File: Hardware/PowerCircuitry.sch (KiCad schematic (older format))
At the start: 37 parts, among them J4 Conn_01x02_Male, Q5 MTP3055VL, Q6 MTP3055VL, Q7 2N2219, SW3 SW_SPST, U4 MAX40200AUK

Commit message: Added lots of things - needs some redoing
Fun, but ffs could have been easier
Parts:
- removed Q7: 2N2219, Package_TO_SOT_THT:TO-92_Inline, symbol Transistor_BJT:2N2219
- removed SW3: SW_SPST, Button_Switch_THT:SW_DIP_SPSTx01_Slide_9.78x4.72mm_W7.62mm_P2.54mm, symbol Switch:SW_SPST
- added J6: Conn_01x02_Male, Connector_PinHeader_2.54mm:PinHeader_1x02_P2.54mm_Vertical, symbol Connector:Conn_01x02_Male
- added JP1: Jumper_2_Open, Connector_PinHeader_2.54mm:PinHeader_1x02_P2.54mm_Vertical, symbol Jumper:Jumper_2_Open
- added Q7: Q_NMOS_GDS, Package_TO_SOT_SMD:SOT-23, symbol Device:Q_NMOS_GDS
- Q5, Q6: footprint Package_TO_SOT_THT:TO-220-3_Vertical -> Package_TO_SOT_SMD:SOT-23
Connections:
- net 12VBusSwitch: now also Q7.1 (G)
- net GND: now also Q7.3 (S); no longer J4.1 (Pin_1)
- net at C1.1.1, L1.1: now also C2.1.1, L2.1, R21.2, U4.5 (OUT)
- net at Battery1.1 (Pin_1): now also J6.2 (Pin_2)
- net at U4.1 (VDD), U4.3 (EN): now also J6.1 (Pin_1)
- new net: J4.1 (Pin_1), JP1.2 (B)
- new net: JP1.1 (A), Q7.2 (D)
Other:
- moved on the sheet: C1.1
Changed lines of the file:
@@
 EESchema Schematic File Version 4
+LIBS:VLAD-cache
 EELAYER 30 0
 EELAYER END
@@
 	0    -1   -1   0
 $EndComp
-Wire Wire Line
-	2950 1250 3150 1250
 $Comp
 L power:GND #PWR036
 U 1 1 607A1CEB
-P 2950 1550
-F 0 "#PWR036" H 2950 1300 50  0001 C CNN
-F 1 "GND" H 2955 1377 50  0000 C CNN
-F 2 "" H 2950 1550 50  0001 C CNN
-F 3 "" H 2950 1550 50  0001 C CNN
-	1    2950 1550
+P 2750 3450
+F 0 "#PWR036" H 2750 3200 50  0001 C CNN
+F 1 "GND" H 2755 3277 50  0000 C CNN
+F 2 "" H 2750 3450 50  0001 C CNN
+F 3 "" H 2750 3450 50  0001 C CNN
+	1    2750 3450
 	1    0    0    -1
 $EndComp
@@
 L Device:CP1 C1.1
 U 1 1 607A0DAB
-P 2950 1400
-F 0 "C1.1" H 3065 1446 50  0000 L CNN
-F 1 "68uF" H 3065 1355 50  0000 L CNN
-F 2 "Capacitor_THT:CP_Radial_D6.3mm_P2.50mm" H 2950 1400 50  0001 C CNN
-F 3 "~" H 2950 1400 50  0001 C CNN
-	1    2950 1400
-	1    0    0    -1
+P 2600 3450
+F 0 "C1.1" H 2715 3496 50  0000 L CNN
+F 1 "68uF" H 2715 3405 50  0000 L CNN
+F 2 "Capacitor_THT:CP_Radial_D6.3mm_P2.50mm" H 2600 3450 50  0001 C CNN
+F 3 "~" H 2600 3450 50  0001 C CNN
+	1    2600 3450
+	0    -1   -1   0
 $EndComp
 $Comp
@@
 L power:GND #PWR055
 U 1 1 609E5451
-P 9050 3100
-F 0 "#PWR055" H 9050 2850 50  0001 C CNN
-F 1 "GND" H 9055 2927 50  0000 C CNN
-F 2 "" H 9050 3100 50  0001 C CNN
-F 3 "" H 9050 3100 50  0001 C CNN
-	1    9050 3100
+P 9050 3900
+F 0 "#PWR055" H 9050 3650 50  0001 C CNN
+F 1 "GND" H 9055 3727 50  0000 C CNN
+F 2 "" H 9050 3900 50  0001 C CNN
+F 3 "" H 9050 3900 50  0001 C CNN
+	1    9050 3900
 	1    0    0    -1
 $EndComp
 Connection ~ 1100 3750
-$Comp
-L Switch:SW_SPST SW3
-U 1 1 608DCB23
-P 1300 3750
-F 0 "SW3" H 1300 3985 50  0000 C CNN
-F 1 "SW_SPST" H 1300 3894 50  0000 C CNN
-F 2 "Button_Switch_THT:SW_DIP_SPSTx01_Slide_9.78x4.72mm_W7.62mm_P2.54mm" H 1300 3750 50  0001 C CNN
-F 3 "~" H 1300 3750 50  0001 C CNN
-	1    1300 3750
-	1    0    0    -1
-$EndComp
 Wire Wire Line
 	2050 3750 2050 4250
@@
 Wire Wire Line
 	4500 3550 4600 3550
-$Comp
-L Transistor_BJT:2N2219 Q7
-U 1 1 60A91052
-P 2550 3250
-F 0 "Q7" H 2741 3204 50  0000 L CNN
-F 1 "2N2219" H 2741 3295 50  0000 L CNN
-F 2 "Package_TO_SOT_THT:TO-92_Inline" H 2750 3175 50  0001 L CIN
-F 3 "http://www.onsemi.com/pub_link/Collateral/2N2219-D.PDF" H 2550 3250 50  0001 L CNN
-	1    2550 3250
-	-1   0    0    1
-$EndComp
 Wire Wire Line
 	2450 3450 2450 3750
-Wire Wire Line
-	2450 3050 2450 1250
-Wire Wire Line
-	2450 1250 2950 1250
-Connection ~ 2950 1250
-Text GLabel 2750 3250 2    50   Input ~ 0
-12VBusSwitch
 $Comp
 L Device:R R21
@@
 F 0 "Q5" H 1400 1770 50  0000 C CNN
 F 1 "MTP3055VL" H 1400 1679 50  0000 C CNN
-F 2 "Package_TO_SOT_THT:TO-220-3_Vertical" H 1400 1500 50  0001 L BNN
+F 2 "Package_TO_SOT_SMD:SOT-23" H 1400 1500 50  0001 L BNN
 F 3 "" H 1400 1500 50  0001 L BNN
 F 4 "MTP3055VL" H 1400 1500 50  0001 L BNN "MPN"
@@
 F 0 "Q6" H 1400 2520 50  0000 C CNN
 F 1 "MTP3055VL" H 1400 2429 50  0000 C CNN
-F 2 "Package_TO_SOT_THT:TO-220-3_Vertical" H 1400 2250 50  0001 L BNN
+F 2 "Package_TO_SOT_SMD:SOT-23" H 1400 2250 50  0001 L BNN
 F 3 "" H 1400 2250 50  0001 L BNN
 F 4 "MTP3055VL" H 1400 2250 50  0001 L BNN "MPN"
@@
 Text Label 4350 4250 1    50   ~ 0
 Source2
+$Comp
+L Connector:Conn_01x02_Male J6
+U 1 1 60AE4D44
+P 1500 3550
+F 0 "J6" V 1562 3594 50  0000 L CNN
+F 1 "Conn_01x02_Male" V 1653 3594 50  0000 L CNN
+F 2 "Connector_PinHeader_2.54mm:PinHeader_1x02_P2.54mm_Vertical" H 1500 3550 50  0001 C CNN
+F 3 "~" H 1500 3550 50  0001 C CNN
+	1    1500 3550
+	0    1    1    0
+$EndComp
+Wire Wire Line
+	1100 3750 1400 3750
+Connection ~ 2450 3450
+Wire Wire Line
+	2450 1250 3150 1250
+Wire Wire Line
+	2450 1250 2450 3450
+$Comp
+L Device:Q_NMOS_GDS Q7
+U 1 1 60B1F303
+P 8950 3700
+F 0 "Q7" H 9156 3746 50  0000 L CNN
+F 1 "Q_NMOS_GDS" H 9156 3655 50  0000 L CNN
+F 2 "Package_TO_SOT_SMD:SOT-23" H 9150 3800 50  0001 C CNN
+F 3 "~" H 8950 3700 50  0001 C CNN
+	1    8950 3700
+	1    0    0    -1
+$EndComp
+Text GLabel 8750 3700 0    50   Input ~ 0
+12VBusSwitch
+$Comp
+L Jumper:Jumper_2_Open JP1
+U 1 1 60B321AD
+P 9050 3300
+F 0 "JP1" V 9096 3212 50  0000 R CNN
+F 1 "Jumper_2_Open" V 9005 3212 50  0000 R CNN
+F 2 "Connector_PinHeader_2.54mm:PinHeader_1x02_P2.54mm_Vertical" H 9050 3300 50  0001 C CNN
+F 3 "~" H 9050 3300 50  0001 C CNN
+	1    9050 3300
+	0    -1   -1   0
+$EndComp
 $EndSCHEMATC

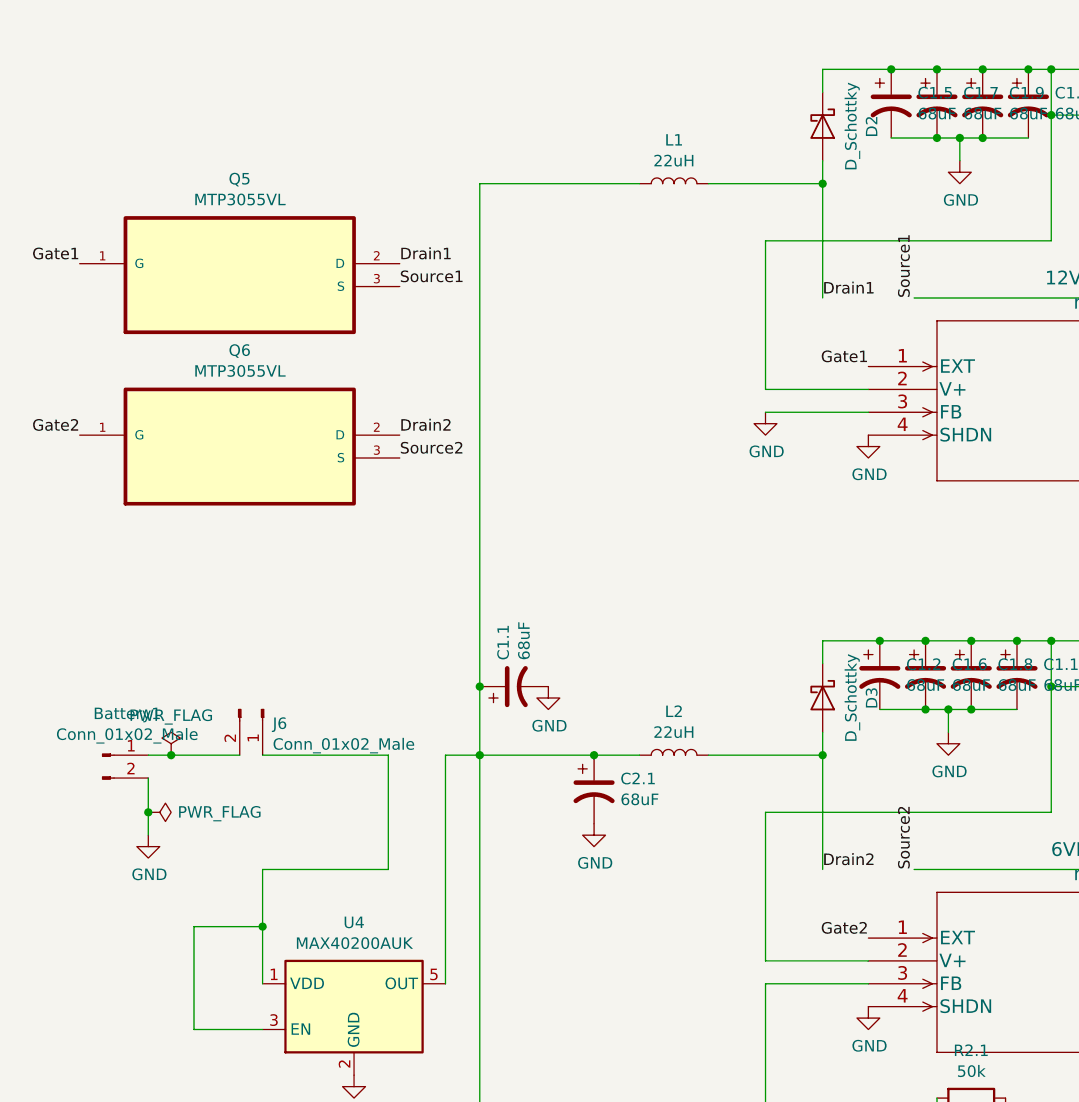
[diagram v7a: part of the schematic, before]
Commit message: Added bunch of vias
Now need to connect some more tracks up and we're good to proceed to adding ground planes etc. Also decreased the size of the board to fit within 90mm x 80mm, have further opportunities to potentially squeeze it.
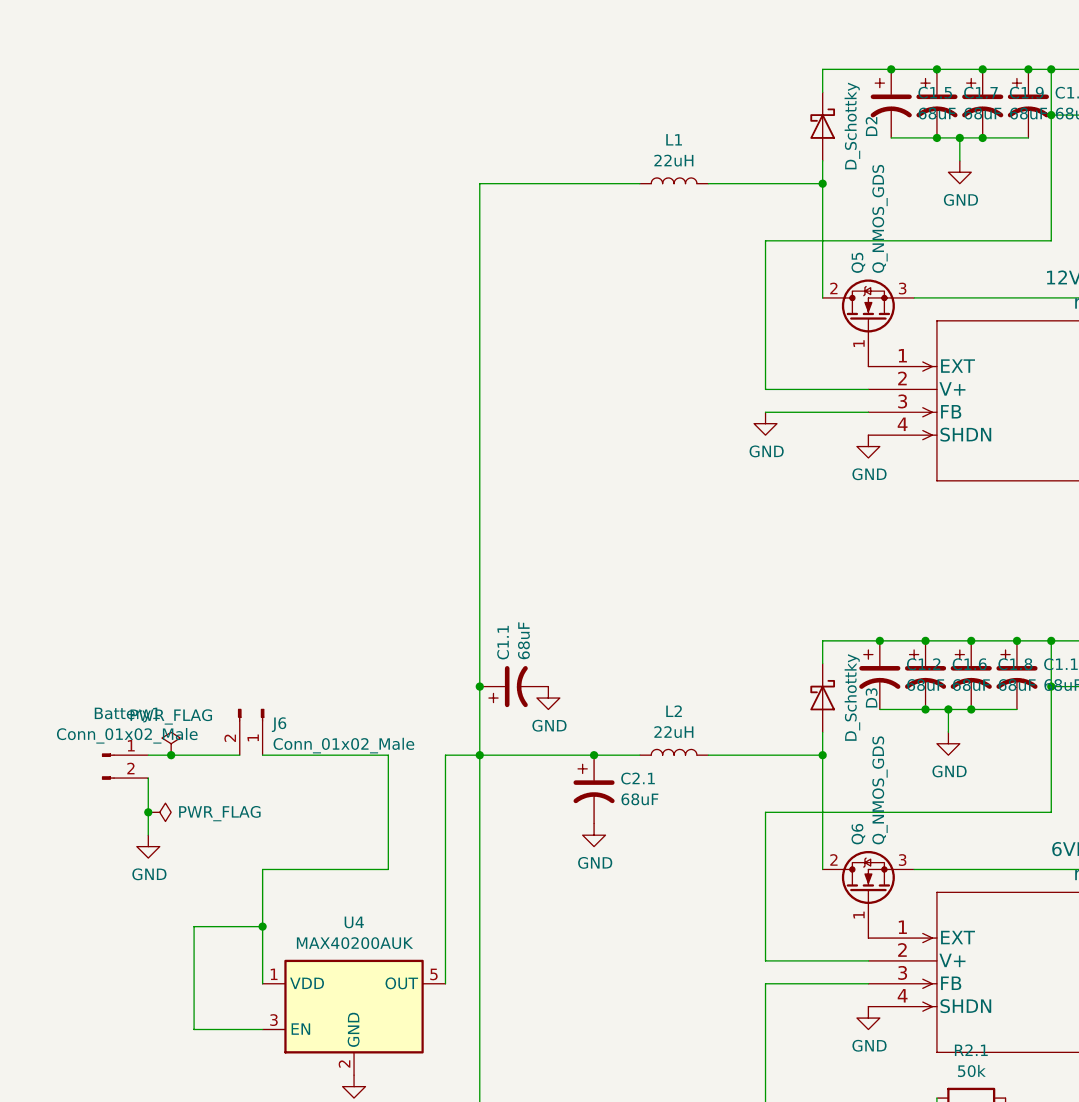
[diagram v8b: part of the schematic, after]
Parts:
- removed Q5, Q6: MTP3055VL, Package_TO_SOT_SMD:SOT-23, symbol VLAD-rescue:MTP3055VL-MTP3055VL
- added Q5, Q6: Q_NMOS_GDS, Package_TO_SOT_SMD:SOT-23, symbol Device:Q_NMOS_GDS
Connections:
- net Drain1: no longer names the net of D2.2 (A), L1.2
- net Drain1: now also Q5.2 (D)
- net Drain2: no longer names the net of D3.2 (A), L2.2
- net Drain2: now also Q6.2 (D)
- net Gate1: no longer names the net of 12VBoostConverter1.1 (EXT)
- net Gate1: now also Q5.1 (G)
- net Gate2: no longer names the net of 6VBoostConverter1.1 (EXT)
- net Gate2: now also Q6.1 (G)
- net Source1: no longer names the net of 12VBoostConverter1.8 (CS), RSense1.1
- net Source1: now also Q5.3 (S)
- net Source2: no longer names the net of 6VBoostConverter1.8 (CS), RSense2.1
- net Source2: now also Q6.3 (S)
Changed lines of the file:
@@
 	2950 6500 3200 6500
-$Comp
-L VLAD-rescue:MTP3055VL-MTP3055VL Q5
-U 1 1 60AA2630
-P 1400 1500
-F 0 "Q5" H 1400 1770 50  0000 C CNN
-F 1 "MTP3055VL" H 1400 1679 50  0000 C CNN
-F 2 "Package_TO_SOT_SMD:SOT-23" H 1400 1500 50  0001 L BNN
-F 3 "" H 1400 1500 50  0001 L BNN
-F 4 "MTP3055VL" H 1400 1500 50  0001 L BNN "MPN"
-F 5 "18C7756" H 1400 1500 50  0001 L BNN "OC_NEWARK"
-F 6 "1845563" H 1400 1500 50  0001 L BNN "OC_FARNELL"
-F 7 "Fairchild" H 1400 1500 50  0001 L BNN "SUPPLIER"
-F 8 "TO-220" H 1400 1500 50  0001 L BNN "PACKAGE"
-	1    1400 1500
-	1    0    0    -1
-$EndComp
-Text Label 700  1600 2    50   ~ 0
-Gate1
-Text Label 4150 2050 2    50   ~ 0
-Gate1
-Text Label 2100 1600 0    50   ~ 0
-Drain1
-Text Label 3950 1750 0    50   ~ 0
-Drain1
-Text Label 2100 1700 0    50   ~ 0
-Source1
-Text Label 4350 1750 1    50   ~ 0
-Source1
-$Comp
-L VLAD-rescue:MTP3055VL-MTP3055VL Q6
-U 1 1 60AC0CD1
-P 1400 2250
-F 0 "Q6" H 1400 2520 50  0000 C CNN
-F 1 "MTP3055VL" H 1400 2429 50  0000 C CNN
-F 2 "Package_TO_SOT_SMD:SOT-23" H 1400 2250 50  0001 L BNN
-F 3 "" H 1400 2250 50  0001 L BNN
-F 4 "MTP3055VL" H 1400 2250 50  0001 L BNN "MPN"
-F 5 "18C7756" H 1400 2250 50  0001 L BNN "OC_NEWARK"
-F 6 "1845563" H 1400 2250 50  0001 L BNN "OC_FARNELL"
-F 7 "Fairchild" H 1400 2250 50  0001 L BNN "SUPPLIER"
-F 8 "TO-220" H 1400 2250 50  0001 L BNN "PACKAGE"
-	1    1400 2250
-	1    0    0    -1
-$EndComp
-Text Label 700  2350 2    50   ~ 0
-Gate2
-Text Label 2100 2350 0    50   ~ 0
-Drain2
-Text Label 2100 2450 0    50   ~ 0
-Source2
-Text Label 4150 4550 2    50   ~ 0
-Gate2
-Text Label 3950 4250 0    50   ~ 0
-Drain2
-Text Label 4350 4250 1    50   ~ 0
-Source2
 $Comp
 L Connector:Conn_01x02_Male J6
@@
 	0    -1   -1   0
 $EndComp
+$Comp
+L Device:Q_NMOS_GDS Q5
+U 1 1 60ADEF8B
+P 4150 1850
+F 0 "Q5" H 4356 1896 50  0000 L CNN
+F 1 "Q_NMOS_GDS" H 4356 1805 50  0000 L CNN
+F 2 "Package_TO_SOT_SMD:SOT-23" H 4350 1950 50  0001 C CNN
+F 3 "~" H 4150 1850 50  0001 C CNN
+	1    4150 1850
+	0    -1   -1   0
+$EndComp
+$Comp
+L Device:Q_NMOS_GDS Q6
+U 1 1 60AE56C5
+P 4150 4350
+F 0 "Q6" H 4356 4396 50  0000 L CNN
+F 1 "Q_NMOS_GDS" H 4356 4305 50  0000 L CNN
+F 2 "Package_TO_SOT_SMD:SOT-23" H 4350 4450 50  0001 C CNN
+F 3 "~" H 4150 4350 50  0001 C CNN
+	1    4150 4350
+	0    -1   -1   0
+$EndComp
